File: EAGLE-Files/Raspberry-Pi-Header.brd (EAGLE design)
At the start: 22.8 x 68.2 mm, 3 parts

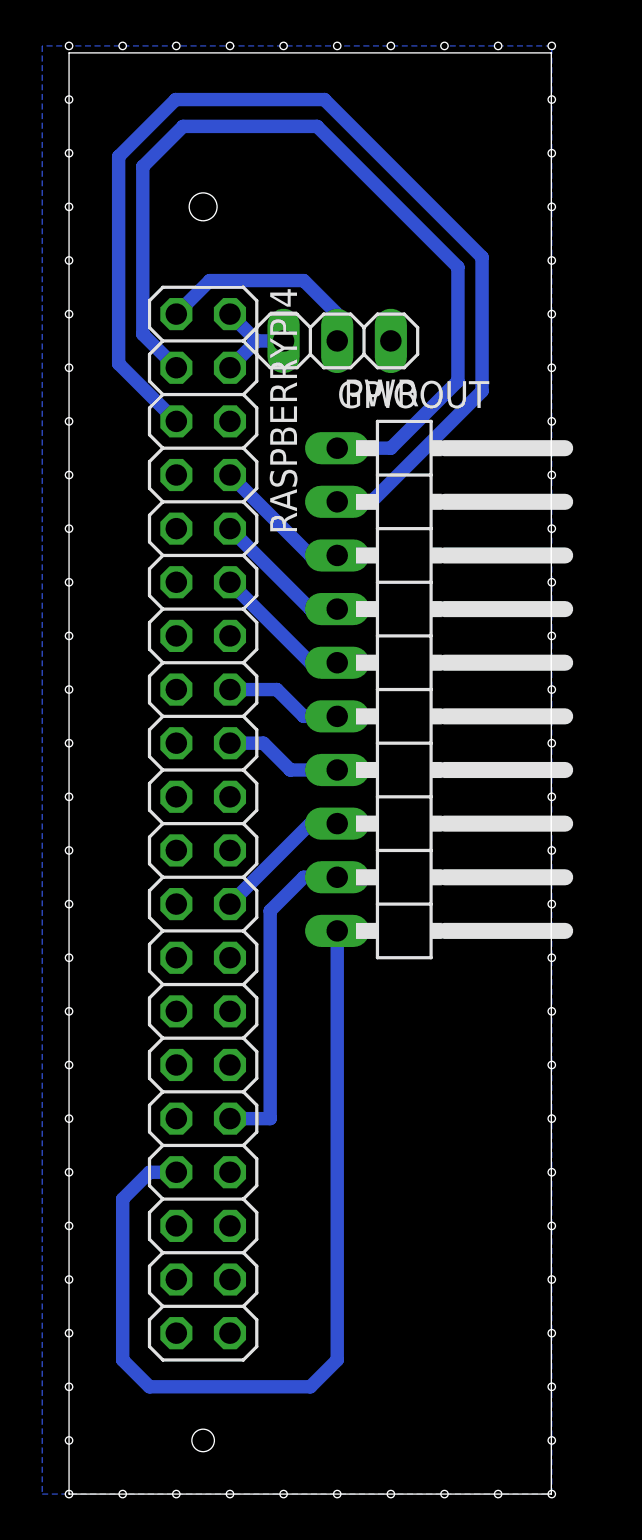
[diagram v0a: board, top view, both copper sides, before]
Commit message: * Updated the header board * Added a audio board * Added a power controller board * Updated gitignore
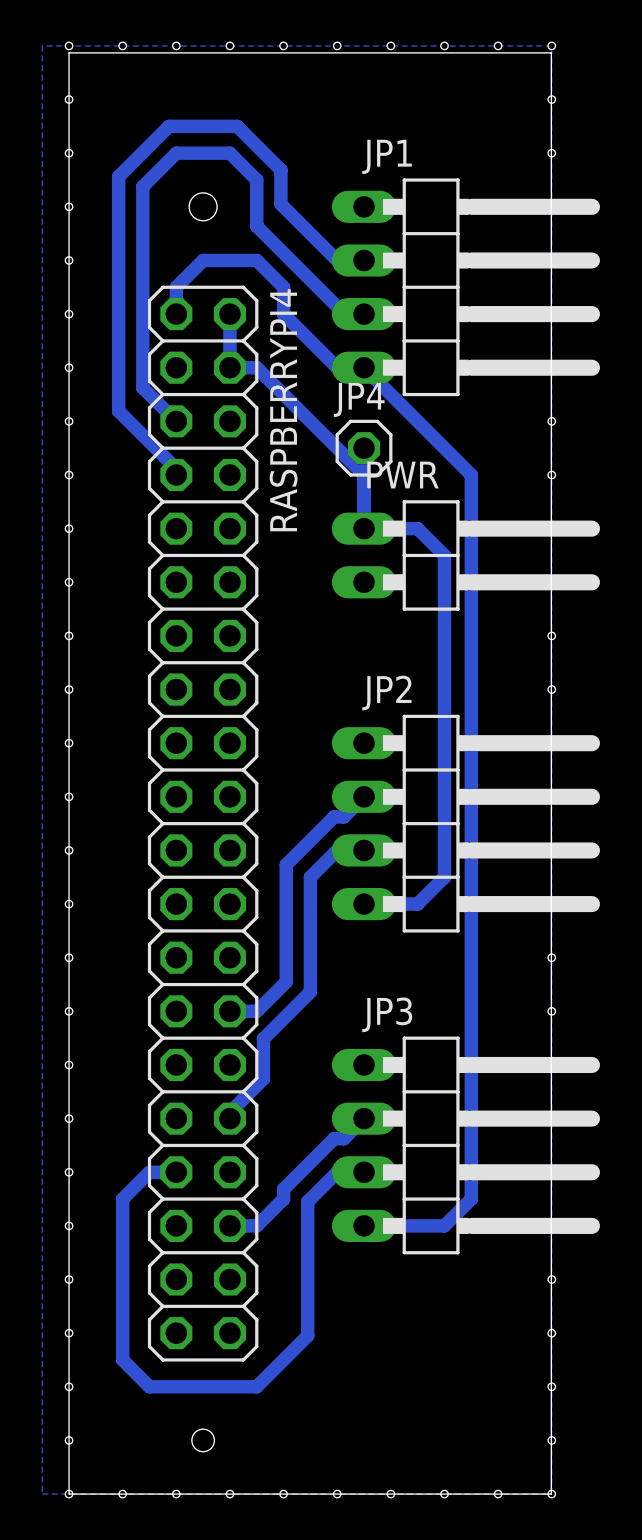
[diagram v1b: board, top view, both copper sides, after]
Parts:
- removed GPIOOUT: (no value), pinhead:1X10/90
- added JP1, JP2, JP3: (no value), pinhead:1X04/90
- added JP4: (no value), pinhead:1X01
- PWR: device pinhead:1X03 -> pinhead:1X02/90
- moved PWR 11.4 mm to (17.8, 44.5), turned to 270 degrees
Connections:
- removed net GPIO14: GPIOOUT.3, RASPBERRYPI4.8
- removed net GPIO15: GPIOOUT.4, RASPBERRYPI4.10
- removed net GPIO18: GPIOOUT.5, RASPBERRYPI4.12
- removed net GPIO23: GPIOOUT.6, RASPBERRYPI4.16
- removed net GPIO24: GPIOOUT.7, RASPBERRYPI4.18
- removed net GPIO8: GPIOOUT.8, RASPBERRYPI4.24
- new net GPIO1: JP2.2, RASPBERRYPI4.28
- new net GPIO16: JP3.2, RASPBERRYPI4.36
- net +3V3: now also JP1.4, JP3.4; no longer PWR.2
- net +5V: now also JP2.4, JP4.1, PWR.1; no longer PWR.3
- net GND: now also JP1.1, JP2.1, JP3.1, PWR.2; no longer PWR.1
- net GPIO12: now also JP2.3; no longer GPIOOUT.9
- net GPIO13: now also JP3.3; no longer GPIOOUT.10
- net SCL: now also JP1.2, RASPBERRYPI4.7; no longer GPIOOUT.2, RASPBERRYPI4.5
- net SDA: now also JP1.3, RASPBERRYPI4.5; no longer GPIOOUT.1, RASPBERRYPI4.3
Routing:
- net +3V3: track 10.2 -> 60.6 mm
- net +5V: track 4.86 -> 41.3 mm
- net SCL: track 50.5 -> 31.4 mm
- net GPIO1: track 0.00 -> 13.8 mm
- net SDA: track 41.1 -> 27.3 mm
- net GPIO13: track 42.2 -> 30.6 mm
- net GPIO16: track 0.00 -> 8.73 mm
- net GPIO18: track 6.66 -> 0.00 mm
- net GPIO15: track 6.66 -> 0.00 mm
- net GPIO8: track 6.66 -> 0.00 mm
- net GPIO14: track 6.66 -> 0.00 mm
- net GPIO24: track 5.61 -> 0.00 mm
- net GPIO23: track 5.61 -> 0.00 mm

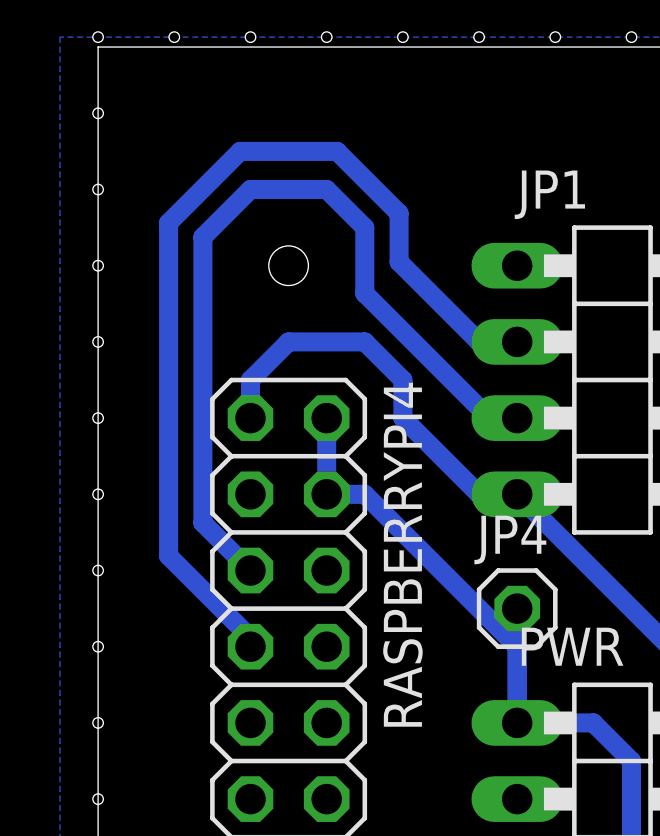
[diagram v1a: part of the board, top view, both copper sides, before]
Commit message: * Fixed a small error in the Raspberry Pi GPIO Header board (pins was offset) * Added the initial 3d print files
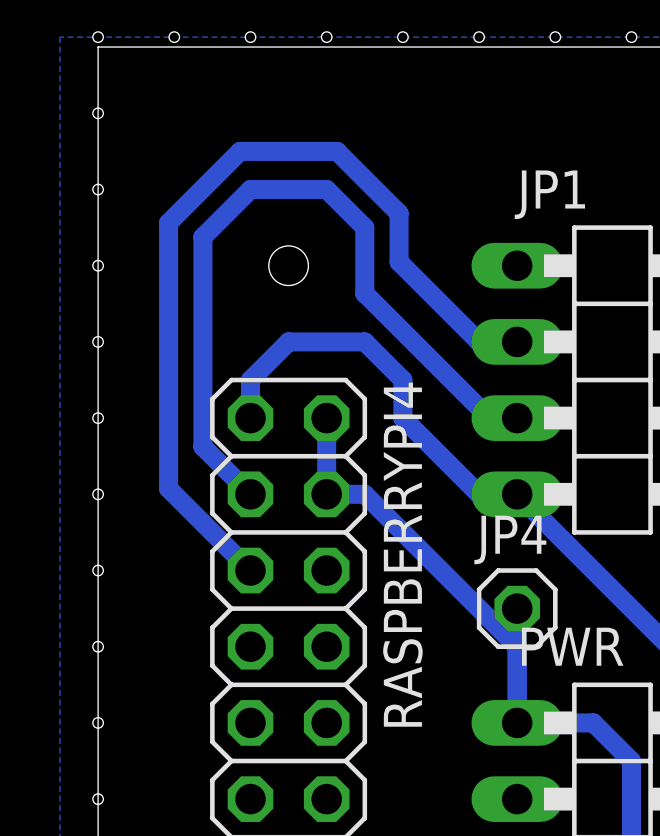
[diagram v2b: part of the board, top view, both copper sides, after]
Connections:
- net SCL: now also RASPBERRYPI4.5; no longer RASPBERRYPI4.7
- net SDA: now also RASPBERRYPI4.3; no longer RASPBERRYPI4.5
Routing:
- net SDA: track 27.3 -> 24.8 mm
- net SCL: track 31.4 -> 28.9 mm
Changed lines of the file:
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@@
 </class>
 </classes>
-<designrules name="default2">
+<designrules name="default2 *">
 <description language="de">&lt;b&gt;EAGLE Design Rules&lt;/b&gt;
 &lt;p&gt;
@@
 <param name="mdSmdStop" value="0mil"/>
 <param name="msWidth" value="25mil"/>
-<param name="msDrill" value="0.35mm"/>
+<param name="msDrill" value="0.45mm"/>
 <param name="msMicroVia" value="9.99mm"/>
 <param name="msBlindViaRatio" value="0.5"/>
@@
 <signal name="SCL">
 <contactref element="JP1" pad="2"/>
-<contactref element="RASPBERRYPI4" pad="7"/>
-<wire x1="5.08" y1="48.55493125" x2="5.08" y2="48.26" width="0.635" layer="16"/>
-<wire x1="2.3495" y1="51.28543125" x2="5.08" y2="48.55493125" width="0.635" layer="16"/>
 <wire x1="13.97" y1="58.42" x2="12.7" y2="58.42" width="0.635" layer="16"/>
 <wire x1="10.033" y1="61.087" x2="10.033" y2="62.70345" width="0.635" layer="16"/>
@@
 <wire x1="7.96645" y1="64.77" x2="4.73355" y2="64.77" width="0.635" layer="16"/>
 <wire x1="4.73355" y1="64.77" x2="2.3495" y2="62.38595" width="0.635" layer="16"/>
-<wire x1="2.3495" y1="62.38595" x2="2.3495" y2="51.28543125" width="0.635" layer="16"/>
+<contactref element="RASPBERRYPI4" pad="5"/>
+<wire x1="2.3495" y1="62.38595" x2="2.3495" y2="53.5305" width="0.635" layer="16"/>
+<wire x1="2.3495" y1="53.5305" x2="5.08" y2="50.8" width="0.635" layer="16"/>
 </signal>
 <signal name="SDA">
-<contactref element="RASPBERRYPI4" pad="5"/>
 <contactref element="JP1" pad="3"/>
-<wire x1="5.08" y1="50.8" x2="3.4925" y2="52.3875" width="0.635" layer="16"/>
-<wire x1="3.4925" y1="52.3875" x2="3.4925" y2="61.9125" width="0.635" layer="16"/>
-<wire x1="3.4925" y1="61.9125" x2="5.08" y2="63.5" width="0.635" layer="16"/>
+<wire x1="5.08" y1="63.5" x2="3.4925" y2="61.9125" width="0.635" layer="16"/>
 <wire x1="5.08" y1="63.5" x2="7.62" y2="63.5" width="0.635" layer="16"/>
 <wire x1="8.89" y1="62.23" x2="7.62" y2="63.5" width="0.635" layer="16"/>
@@
 <wire x1="8.89" y1="60.03645" x2="8.89" y2="62.23" width="0.635" layer="16"/>
 <wire x1="13.04645" y1="55.88" x2="8.89" y2="60.03645" width="0.635" layer="16"/>
+<contactref element="RASPBERRYPI4" pad="3"/>
+<wire x1="3.4925" y1="54.9275" x2="5.08" y2="53.34" width="0.635" layer="16"/>
+<wire x1="3.4925" y1="61.9125" x2="3.4925" y2="54.9275" width="0.635" layer="16"/>
 </signal>
 <signal name="GPIO13">
